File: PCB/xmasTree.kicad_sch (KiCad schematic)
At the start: 37 parts, among them J1 USB_B_Micro, J2 Conn_01x05, J3 Conn_01x05, J4 Conn_01x05, J5 Conn_01x04, Q1 BSS138, U1 LD1117S33TR_SOT223, U2 ESP32-WROOM-32

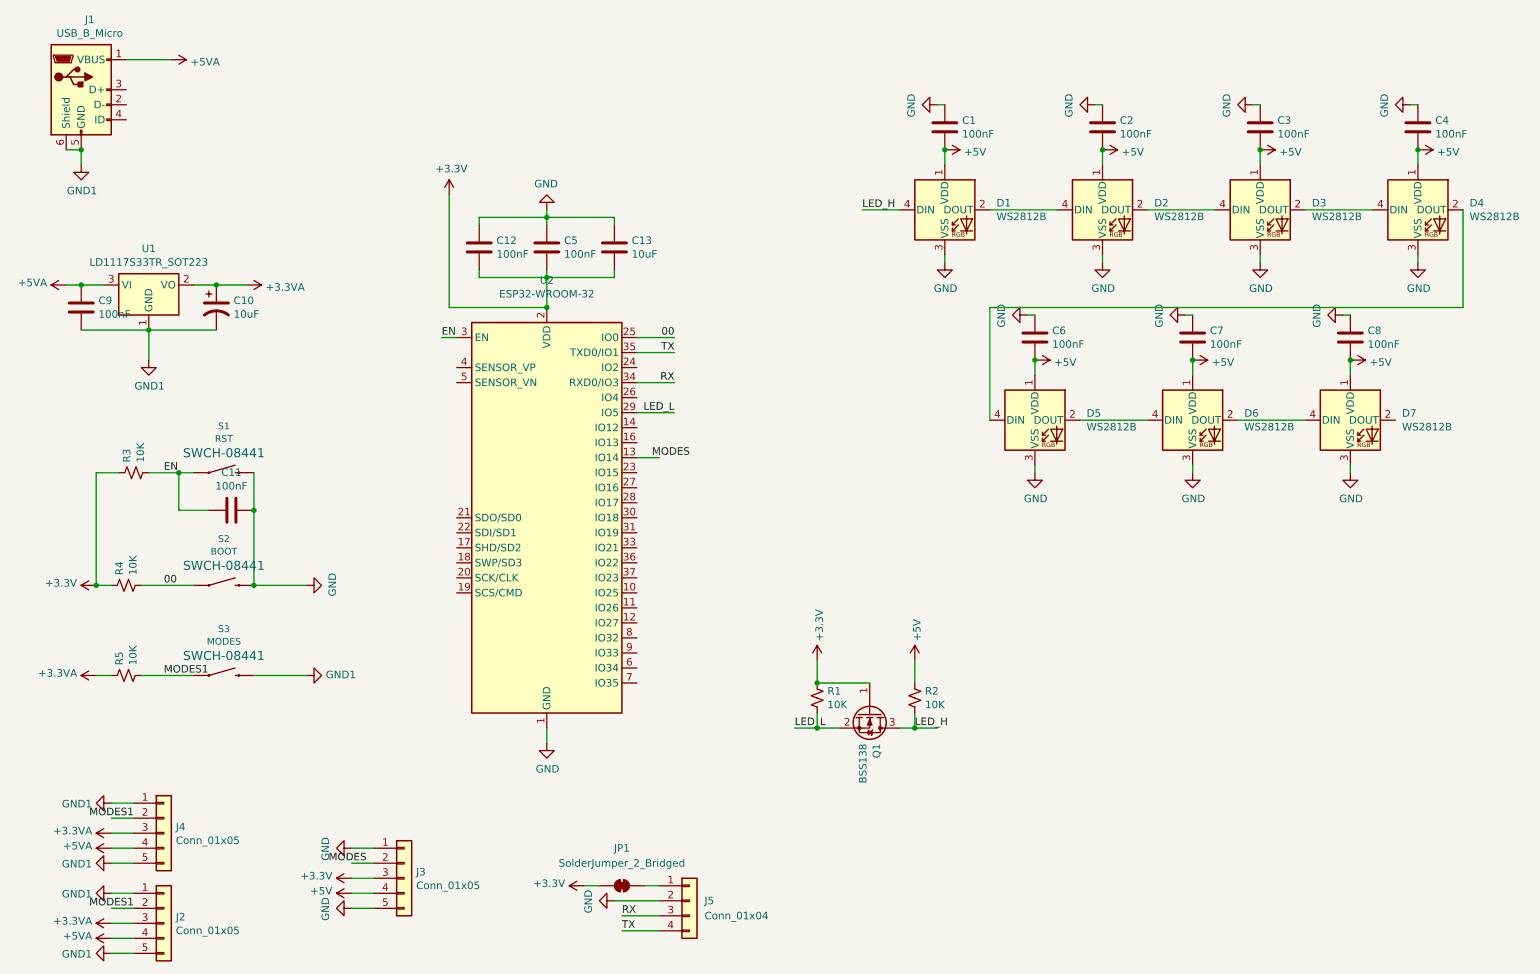
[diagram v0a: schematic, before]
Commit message: Updated to R2 4pin buttons were connected wrong. Swapped them to 2pin narrow version at the same time.
Signed-off-by: theloukou <lefteriskantakos@yahoo.com>
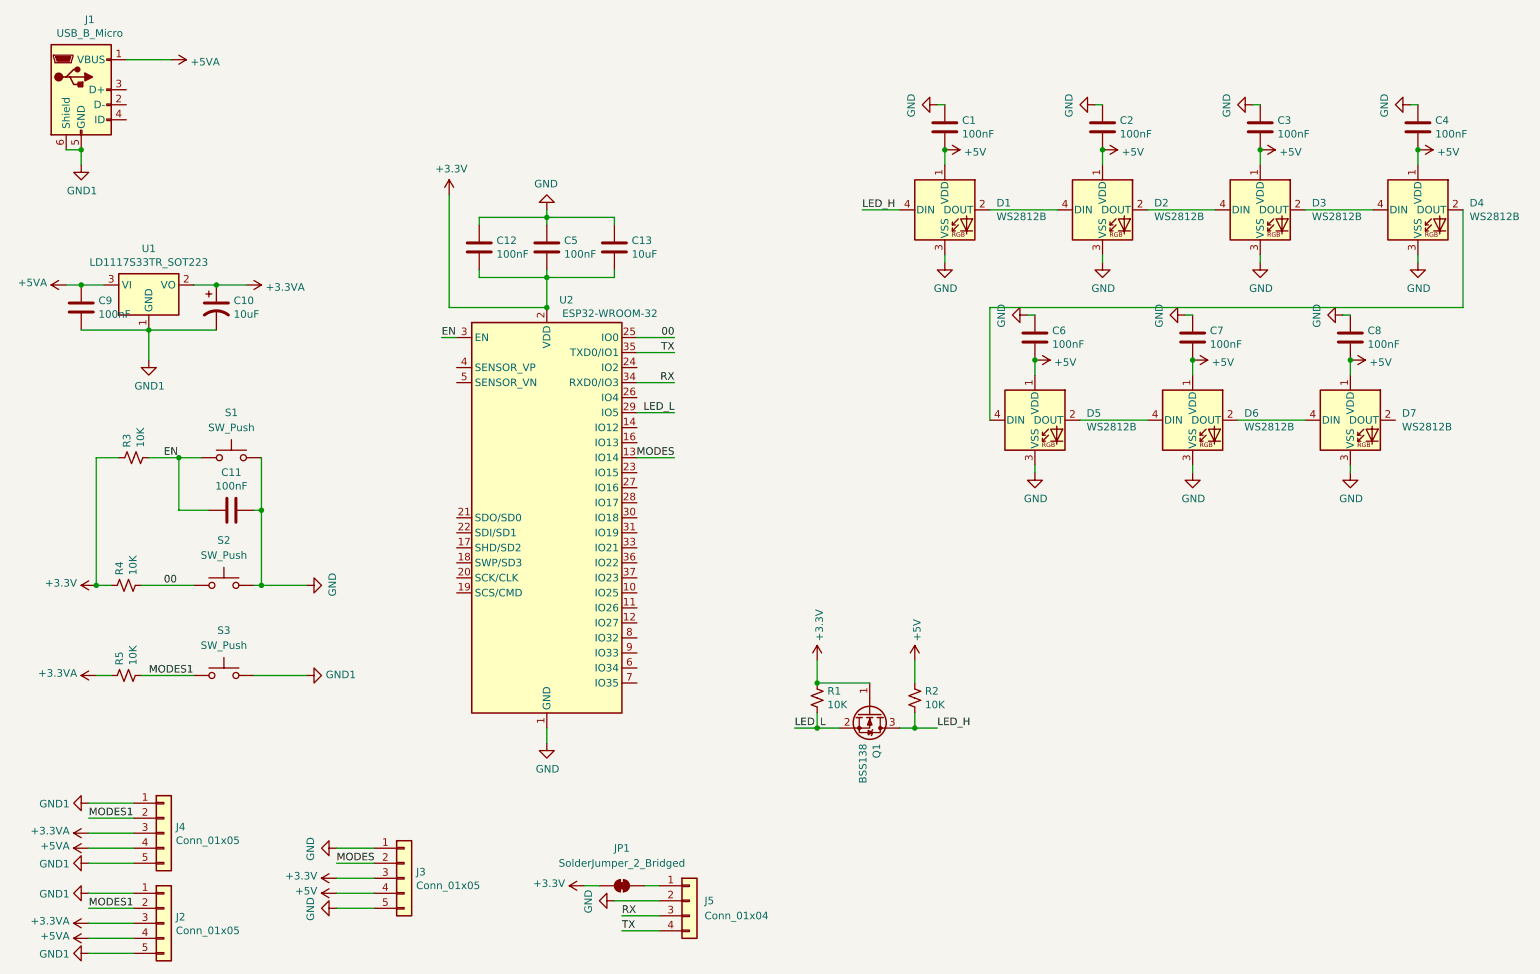
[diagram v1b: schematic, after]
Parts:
- removed S1: RST, Switches:TACTILE_SWITCH_PTH_6.0MM, symbol SparkFun-Switches:MOMENTARY-SWITCH-SPST-PTH-6.0MM
- removed S2: BOOT, Switches:TACTILE_SWITCH_PTH_6.0MM, symbol SparkFun-Switches:MOMENTARY-SWITCH-SPST-PTH-6.0MM
- removed S3: MODES, Switches:TACTILE_SWITCH_PTH_6.0MM, symbol SparkFun-Switches:MOMENTARY-SWITCH-SPST-PTH-6.0MM
- added S1, S2, S3: SW_Push, Button_Switch_THT:SW_PUSH_1P1T_6x3.5mm_H4.3_APEM_MJTP1243, symbol Switch:SW_Push
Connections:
- net 00: now also S2.1
- net EN: now also S1.1
- net GND: now also S1.2, S2.2
- net GND1: now also S3.2
- net MODES1: now also S3.1
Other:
- moved on the sheet: R3
